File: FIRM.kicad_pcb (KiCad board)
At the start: 4 copper layers, 40.5 x 40.5 mm, 98 parts, among them J2 DM3CS-SF, Q2 IRLML6402, U1 STM32F405RGTx, U2 MIC5219-3.3YM5, U6 A-USBC-20F0-EA-GSR05, U7 W25Q128JVS, X2 32.768khz, Y1 12 MHz

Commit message: sub 600
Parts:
- removed 3.3V: 3.3V Test Point, TestPoint:TestPoint_THTPad_1.5x1.5mm_Drill0.7mm
- removed A0: PA0 Test Point, TestPoint:TestPoint_THTPad_1.5x1.5mm_Drill0.7mm
- removed A1: PA1 Test Point, TestPoint:TestPoint_THTPad_1.5x1.5mm_Drill0.7mm
- removed A10: PA10 Test Point, TestPoint:TestPoint_THTPad_1.5x1.5mm_Drill0.7mm
- removed A15: PA15 Test Point, TestPoint:TestPoint_THTPad_1.5x1.5mm_Drill0.7mm
- removed A2: PA2 Test Point, TestPoint:TestPoint_THTPad_1.5x1.5mm_Drill0.7mm
- removed A3: PA3 Test Point, TestPoint:TestPoint_THTPad_1.5x1.5mm_Drill0.7mm
- removed A4: PA4 Test Point, TestPoint:TestPoint_THTPad_1.5x1.5mm_Drill0.7mm
- removed A8: PA8 Test Point, TestPoint:TestPoint_THTPad_1.5x1.5mm_Drill0.7mm
- removed A9: PA9 Test Point, TestPoint:TestPoint_THTPad_1.5x1.5mm_Drill0.7mm
- removed B10: PB10 Test Point, TestPoint:TestPoint_THTPad_1.5x1.5mm_Drill0.7mm
- removed B11: PB11 Test Point, TestPoint:TestPoint_THTPad_1.5x1.5mm_Drill0.7mm
- removed B3: PB3 Test Point, TestPoint:TestPoint_THTPad_1.5x1.5mm_Drill0.7mm
- removed B4: PB4 Test Point, TestPoint:TestPoint_THTPad_1.5x1.5mm_Drill0.7mm
- removed B5: PB5 Test Point, TestPoint:TestPoint_THTPad_1.5x1.5mm_Drill0.7mm
- removed B8: PB8 Test Point, TestPoint:TestPoint_THTPad_1.5x1.5mm_Drill0.7mm
- removed BAT: Conn_01x02_Pin, Connector_PinHeader_2.54mm:PinHeader_1x02_P2.54mm_Vertical
- removed BOOT0: BOOT0 Pad, TestPoint:TestPoint_Pad_1.5x1.5mm
- removed C0: PC0 Test Point, TestPoint:TestPoint_THTPad_1.5x1.5mm_Drill0.7mm
- removed the C13 at (101.5, 107.0)
- removed the C13 at (117.9, 114.3)
- removed GND (x2): GND Test Point, TestPoint:TestPoint_THTPad_1.5x1.5mm_Drill0.7mm
- removed GND: GND Through-Hole, TestPoint:TestPoint_THTPad_1.5x1.5mm_Drill0.7mm
- removed MOSI: SPI_SDI, Jumper:SolderJumper-2_P1.3mm_Open_RoundedPad1.0x1.5mm
- removed Q2: IRLML6402, Package_TO_SOT_SMD:SOT-23
- removed R22: 5.1k, Resistor_SMD:R_0603_1608Metric
- removed RST: PTS815, Button_Switch_SMD:SW_SPST_PTS810
- removed SCK: SPI_SCK, Jumper:SolderJumper-2_P1.3mm_Open_RoundedPad1.0x1.5mm
- removed SCL: I2C_SCL, Jumper:SolderJumper-2_P1.3mm_Open_RoundedPad1.0x1.5mm
- removed SDA: I2C_SDA, Jumper:SolderJumper-2_P1.3mm_Open_RoundedPad1.0x1.5mm
- removed SWCLK: SWCLK Through-Hole, TestPoint:TestPoint_THTPad_1.5x1.5mm_Drill0.7mm
- removed SWDIO: SWDIO Through-Hole, TestPoint:TestPoint_THTPad_1.5x1.5mm_Drill0.7mm
- removed TP30: PC1 Test Point, TestPoint:TestPoint_THTPad_1.5x1.5mm_Drill0.7mm
- removed X2: 32.768khz, Crystal:Crystal_SMD_3215-2Pin_3.2x1.5mm
- added C13: 100n, Capacitor_SMD:C_0402_1005Metric, F.Cu at (126.0, 68.8)
- added C28: 10u, Capacitor_SMD:C_0402_1005Metric, F.Cu at (131.5, 83.4)
- added C29: 1u, Capacitor_SMD:C_0402_1005Metric, F.Cu at (131.5, 85.3)
- added C30: 10u, Capacitor_SMD:C_0402_1005Metric, F.Cu at (131.5, 87.3)
- added J1: DM3CS-SF, connectors:HRS_DM3CS-SF, B.Cu at (160.7, 88.9)
- added Q1: IRLML6402, Package_TO_SOT_SMD:SOT-23, F.Cu at (165.5, 94.0)
- added R16: 100k, Resistor_SMD:R_0402_1005Metric, F.Cu at (131.8, 91.3)
- added R17: 0.01R, Resistor_SMD:R_0402_1005Metric, F.Cu at (131.8, 93.3)
- added TP1: PA0 Test Point, connectors:Testpoint_1.5x1.5mm_1.0mm, F.Cu at (173.7, 75.7)
- added TP10: I2C1_SCL Test Point, connectors:smd_test_pads_1mm, F.Cu at (136.6, 89.4)
- added TP11: I2C1_SDA Test Point, connectors:smd_test_pads_1mm, F.Cu at (136.6, 91.6)
- added TP12: SWDIO Through-Hole, connectors:Testpoint_1.5x1.5mm_1.0mm, F.Cu at (173.7, 85.9)
- added TP13: SWCLK Through-Hole, connectors:Testpoint_1.5x1.5mm_1.0mm, F.Cu at (173.7, 83.3)
- added TP14: 3.3V Test Point, connectors:Testpoint_1.5x1.5mm_1.0mm, F.Cu at (173.7, 96.0)
- added TP15: GND Test Point, connectors:Testpoint_1.5x1.5mm_1.0mm, F.Cu at (173.7, 88.4)
- added TP16: IMU_CS Test Point, connectors:smd_test_pads_1mm, F.Cu at (136.6, 93.9)
- added TP17: BMP_CS Test Point, connectors:smd_test_pads_1mm, F.Cu at (136.6, 96.1)
- added TP18: MAG_CS Test Point, connectors:smd_test_pads_1mm, F.Cu at (138.8, 89.4)
- added TP19: HIG_CS Test Point, connectors:smd_test_pads_1mm, F.Cu at (138.8, 91.6)
- added TP2: PA1 Test Point, connectors:Testpoint_1.5x1.5mm_1.0mm, F.Cu at (173.7, 78.3)
- added TP20: IMU_INT Test Point, connectors:smd_test_pads_1mm, F.Cu at (138.8, 93.9)
- added TP21: BMP_INT Test Point, connectors:smd_test_pads_1mm, F.Cu at (138.8, 96.1)
- added TP22: MAG_INT Test Point, connectors:smd_test_pads_1mm, F.Cu at (141.1, 89.4)
- added TP23: HIG_INT Test Point, connectors:smd_test_pads_1mm, F.Cu at (141.1, 91.6)
- added TP24: NRST Pad, connectors:smd_test_pads_1mm, F.Cu at (141.1, 93.9)
- added TP25: BOOT0 Pad, connectors:smd_test_pads_1mm, F.Cu at (141.1, 96.1)
- added TP3: PA2 Test Point, connectors:Testpoint_1.5x1.5mm_1.0mm, F.Cu at (173.7, 80.8)
- added TP4: PA9 Test Point, connectors:Testpoint_1.5x1.5mm_1.0mm, F.Cu at (173.7, 93.5)
- added TP5: PA10 Test Point, connectors:Testpoint_1.5x1.5mm_1.0mm, F.Cu at (173.7, 91.0)
- added TP6: PA4 Test Point, connectors:smd_test_pads_1mm, F.Cu at (134.4, 89.4)
- added TP7: MOSI2 Test Point, connectors:smd_test_pads_1mm, F.Cu at (134.4, 91.6)
- added TP8: MISO2 Test Point, connectors:smd_test_pads_1mm, F.Cu at (134.4, 93.9)
- added TP9: SCK2 Test Point, connectors:smd_test_pads_1mm, F.Cu at (134.4, 96.1)
- added U8: ~, sensors:IC_MMC5983MA, F.Cu at (170.8, 78.5)
- added U9: A-USBC-20F0-EA-GSR05, connectors:A-USBC-20F0-EA-GSR05, F.Cu at (163.9, 100.5)
- added X1: 32.768khz, Crystal:Crystal_SMD_3215-2Pin_3.2x1.5mm, F.Cu at (159.1, 75.8)
- C1: value 100n -> 0.1u; footprint Capacitor_SMD:C_0603_1608Metric -> Capacitor_SMD:C_0402_1005Metric
- C10: value 2u2 -> 14p; footprint Capacitor_SMD:C_0603_1608Metric -> Capacitor_SMD:C_0402_1005Metric
- C11, C12: value 6p -> 100n; footprint Capacitor_SMD:C_0603_1608Metric -> Capacitor_SMD:C_0402_1005Metric
- C14: value 14p -> 2u2; footprint Capacitor_SMD:C_0603_1608Metric -> Capacitor_SMD:C_0402_1005Metric
- C15, C8: value 0.1u -> 100n; footprint Capacitor_SMD:C_0603_1608Metric -> Capacitor_SMD:C_0402_1005Metric
- C16: value 1u -> 10n; footprint Capacitor_SMD:C_0603_1608Metric -> Capacitor_SMD:C_0402_1005Metric
- C17: value 10u -> 0.1u; footprint Capacitor_SMD:C_0603_1608Metric -> Capacitor_SMD:C_0402_1005Metric
- C18, C19, C20, C21, C24, C25, C27, C3, C9: footprint Capacitor_SMD:C_0603_1608Metric -> Capacitor_SMD:C_0402_1005Metric
- C2: value 100n -> 4u7; footprint Capacitor_SMD:C_0603_1608Metric -> Capacitor_SMD:C_0402_1005Metric
- C22: value 10u -> 100n; footprint Capacitor_SMD:C_0603_1608Metric -> Capacitor_SMD:C_0402_1005Metric
- C23: value 470p -> 100n; footprint Capacitor_SMD:C_0603_1608Metric -> Capacitor_SMD:C_0402_1005Metric
- C26: value 100n -> 470p; footprint Capacitor_SMD:C_0603_1608Metric -> Capacitor_SMD:C_0402_1005Metric
- C4: value 100n -> 6p; footprint Capacitor_SMD:C_0603_1608Metric -> Capacitor_SMD:C_0402_1005Metric
- C5: value 100n -> 14p; footprint Capacitor_SMD:C_0603_1608Metric -> Capacitor_SMD:C_0402_1005Metric
- C6: value 4u7 -> 100n; footprint Capacitor_SMD:C_0603_1608Metric -> Capacitor_SMD:C_0402_1005Metric
- C7: value 10n -> 6p; footprint Capacitor_SMD:C_0603_1608Metric -> Capacitor_SMD:C_0402_1005Metric
- D1: value D_Schottky -> LED_Blue; footprint Diode_SMD:D_SOD-123 -> LED_SMD:LED_0402_1005Metric
- D2: value LED -> LED_Yellow; footprint LED_SMD:LED_0805_2012Metric -> LED_SMD:LED_0402_1005Metric
- D3: value LED -> LED_Red; footprint LED_SMD:LED_0805_2012Metric -> LED_SMD:LED_0402_1005Metric
- D4: value LED -> D_Schottky; footprint LED_SMD:LED_0805_2012Metric -> Diode_SMD:D_SOD-123
- D5: value LED -> LED_Green; footprint LED_SMD:LED_0805_2012Metric -> LED_SMD:LED_0402_1005Metric
- J2: value DM3CS-SF -> Conn_01x02_Pin; footprint DM3CS-SF:HRS_DM3CS-SF -> connectors:power_headers; moved to F.Cu
- R1: value 100k -> 10k; footprint Resistor_SMD:R_0603_1608Metric -> Resistor_SMD:R_0402_1005Metric
- R10: value 330 -> 47k; footprint Resistor_SMD:R_0603_1608Metric -> Resistor_SMD:R_0402_1005Metric
- R11: value 1k2 -> 3k3; footprint Resistor_SMD:R_0603_1608Metric -> Resistor_SMD:R_0402_1005Metric
- R12: value 1k5 -> 3k3; footprint Resistor_SMD:R_0603_1608Metric -> Resistor_SMD:R_0402_1005Metric
- R13: value 10k -> 330; footprint Resistor_SMD:R_0603_1608Metric -> Resistor_SMD:R_0402_1005Metric; moved to B.Cu
- R14: value 10k -> 1k2; footprint Resistor_SMD:R_0603_1608Metric -> Resistor_SMD:R_0402_1005Metric; moved to B.Cu
- R15: value 1k2 -> 1k5; footprint Resistor_SMD:R_0603_1608Metric -> Resistor_SMD:R_0402_1005Metric; moved to B.Cu
- R18: value 2k2 -> 1k2; footprint Resistor_SMD:R_0603_1608Metric -> Resistor_SMD:R_0402_1005Metric
- R19: value 2k2 -> 100; footprint Resistor_SMD:R_0603_1608Metric -> Resistor_SMD:R_0402_1005Metric
- R2, R4, R7: footprint Resistor_SMD:R_0603_1608Metric -> Resistor_SMD:R_0402_1005Metric
- R20: value 100 -> 5.1k; footprint Resistor_SMD:R_0603_1608Metric -> Resistor_SMD:R_0402_1005Metric
- R21: value 10k -> 5.1k; footprint Resistor_SMD:R_0603_1608Metric -> Resistor_SMD:R_0402_1005Metric
- R3: value 47k -> 100k; footprint Resistor_SMD:R_0603_1608Metric -> Resistor_SMD:R_0402_1005Metric
- R5, R6: value 47k -> 10k; footprint Resistor_SMD:R_0603_1608Metric -> Resistor_SMD:R_0402_1005Metric
- R8: value 100k -> 47k; footprint Resistor_SMD:R_0603_1608Metric -> Resistor_SMD:R_0402_1005Metric
- R9: value 5.1k -> 47k; footprint Resistor_SMD:R_0603_1608Metric -> Resistor_SMD:R_0402_1005Metric
- U1: value STM32F405RGTx -> W25Q128JVS; footprint Package_QFP:LQFP-64_10x10mm_P0.5mm -> Package_SO:SOIC-8_5.3x5.3mm_P1.27mm; moved to B.Cu
- U2: value MIC5219-3.3YM5 -> STM32F405RGTx; footprint Package_TO_SOT_SMD:SOT-23-5 -> Package_QFP:LQFP-64_10x10mm_P0.5mm
- U3: value ~ -> ADXL371; footprint sensors:IC_ICM-45686 -> Sensor_Motion:Analog_LGA-16_3.25x3mm_P0.5mm_LayoutBorder3x5y
- U4: footprint sensors:IC_MMC5983MA -> sensors:IC_ICM-45686
- U5: value ~ -> INA219AxDCN; footprint Package_LGA:ST_HLGA-10_2x2mm_P0.5mm_LayoutBorder3x2y -> Package_TO_SOT_SMD:SOT-23-8
- U6: value A-USBC-20F0-EA-GSR05 -> MIC5219-3.3YM5; footprint connectors:A-USBC-20F0-EA-GSR05 -> Package_TO_SOT_SMD:SOT-23-5
- U7: value W25Q128JVS -> ~; footprint Package_SO:SOIC-8_5.3x5.3mm_P1.27mm -> sensors:BMPFootprintNoSolderMask; moved to F.Cu
- moved U4 76.6 mm to (171.3, 89.5), turned to 135 degrees
- moved H1 76.3 mm to (165.8, 77.1)
- moved D2 70.7 mm to (162.1, 76.1), turned to 0 degrees
- moved D3 69.2 mm to (162.0, 75.2), turned to 0 degrees
- moved H3 69.1 mm to (172.0, 99.1)
- moved R15 65.5 mm to (165.6, 80.1), turned to 0 degrees
- moved U3 64.0 mm to (170.7, 84.7), turned to -135 degrees
- moved J2 63.7 mm to (172.0, 93.0), turned to 0 degrees
- moved D1 63.1 mm to (162.1, 77.0)
- moved D5 59.9 mm to (166.9, 92.1), turned to 90 degrees
- moved C19 58.2 mm to (128.6, 77.5), turned to 0 degrees
- moved D4 56.3 mm to (161.0, 94.8), turned to 0 degrees
- moved C22 55.0 mm to (128.6, 83.4), turned to 0 degrees
- moved U5 54.2 mm to (169.2, 93.7), turned to 90 degrees
- moved C26 53.5 mm to (131.5, 79.4), turned to 0 degrees
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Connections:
- C1 pad 1: +3.3V -> /NRST
- C10 pad 1: /VCAP2 -> /HSE_OUT
- C11 pad 1: /LSE_IN -> GND
- C11 pad 2: GND -> +3.3V
- C12 pad 1: /LSE_OUT -> GND
- C12 pad 2: GND -> +3.3V
- C14 pad 1: /HSE_OUT -> /VCAP2
- C15 pad 1: /NRST -> +3.3V
- C16 pad 1: +3.3V -> Net-(U2-VDDA)
- C17 pad 1: GND -> Net-(U2-VDDA)
- C17 pad 2: Net-(U4-CAP) -> GND
- C19 pad 1: +3.3V -> GND
- C19 pad 2: GND -> +3.3V
- C20 pad 1: +3.3V -> GND
- C20 pad 2: GND -> +3.3V
- C21 pad 1: GND -> +3.3V
- C21 pad 2: +3.3V -> GND
- C22 pad 1: Net-(D1-K) -> +3.3V
- C23 pad 1: Net-(U2-BP) -> GND
- C23 pad 2: GND -> +3.3V
- C24 pad 1: +3.3V -> /VSENS_OUT
- C26 pad 1: GND -> Net-(U6-BP)
- C26 pad 2: +3.3V -> GND
- C4 pad 1: +3.3V -> /LSE_IN
- C5 pad 1: +3.3V -> /HSE_IN
- C7 pad 1: Net-(U1-VDDA) -> /LSE_OUT
- C8 pad 1: Net-(U1-VDDA) -> +3.3V
- D1 pad 1: Net-(D1-K) -> GND
- D1 pad 2: VBUS -> Net-(D1-A)
- D4 pad 1: GND -> /VSENS_IN
- D4 pad 2: Net-(D4-A) -> VBUS
- FB1 pad 1: Net-(U1-VDDA) -> Net-(U2-VDDA)
- J2 pad 1: /SDIO_D2 -> VBAT
- J2 pad 2: /SDIO_D3 -> GND
- R1 pad 1: /BOOT0 -> +3.3V
- R1 pad 2: GND -> Net-(U1-~{HOLD}/~{RESET}/IO_{3})
- R10 pad 1: Net-(D2-A) -> /SDIO_D2
- R10 pad 2: /DBUG_0 -> +3.3V
- R11 pad 1: Net-(D3-A) -> /I2C1_SCL
- R11 pad 2: /DBUG_1 -> +3.3V
- R12 pad 1: Net-(D4-A) -> /I2C1_SDA
- R12 pad 2: /DBUG_2 -> +3.3V
- R13 pad 1: +3.3V -> Net-(D1-A)
- R13 pad 2: Net-(U7-~{HOLD}/~{RESET}/IO_{3}) -> /DBUG_0
- R14 pad 1: +3.3V -> Net-(D2-A)
- R14 pad 2: Net-(U7-~{WP}/IO_{2}) -> /DBUG_1
- R15 pad 1: Net-(D5-A) -> Net-(D3-A)
- R15 pad 2: +3.3V -> /DBUG_2
- R18 pad 1: /I2C1_SCL -> Net-(D5-A)
- R19 pad 1: /I2C1_SDA -> Net-(R19-Pad1)
- R19 pad 2: +3.3V -> /BOOT0
- R2 pad 1: /SDIO_D2 -> /SDIO_D1
- R20 pad 2: /BOOT0 -> GND
- R21 pad 1: +3.3V -> Net-(U9-CC2)
- R21 pad 2: /FLASH_CS -> GND
- R3 pad 1: /SDIO_D3 -> /BOOT0
- R3 pad 2: +3.3V -> GND
- R4 pad 1: /SDIO_CMD -> /SDIO_D0
- R5 pad 1: /SDIO_D0 -> +3.3V
- R5 pad 2: +3.3V -> Net-(U1-~{WP}/IO_{2})
- R6 pad 1: /SDIO_D1 -> +3.3V
- R6 pad 2: +3.3V -> /SD_DETECT
- R7 pad 2: /SD_DETECT -> /FLASH_CS
- R8 pad 1: VBUS -> /SDIO_CMD
- R8 pad 2: GND -> +3.3V
- R9 pad 1: Net-(U6-CC1) -> /SDIO_D3
- R9 pad 2: GND -> +3.3V
- U1 pad 1: +3.3V -> /FLASH_CS
- U1 pad 2: /PC13 -> /MISO1
- U1 pad 3: /LSE_IN -> Net-(U1-~{WP}/IO_{2})
- U1 pad 4: /LSE_OUT -> GND
- U1 pad 5: /HSE_IN -> /MOSI1
- U1 pad 6: /HSE_OUT -> /SCK1
- U1 pad 7: /NRST -> Net-(U1-~{HOLD}/~{RESET}/IO_{3})
- U1 pad 8: /PC0 -> +3.3V
- U2 pad 1: Net-(D1-K) -> +3.3V
- U2 pad 2: GND -> /PC13
- U2 pad 3: Net-(D1-K) -> /LSE_IN
- U2 pad 4: Net-(U2-BP) -> /LSE_OUT
- U2 pad 5: +3.3V -> /HSE_IN
- U3 pad 1: /MISO2 -> +3.3V
- U3 pad 11: unconnected-(U3-RESV/AUX1_SDO-Pad11) -> /HIG_INT
- U3 pad 12: /IMU_CS -> GND
- U3 pad 13: /SCK2 -> GND
- U3 pad 14: /MOSI2 -> +3.3V
- U3 pad 4: /IMU_INT -> /SCK2
- U3 pad 5: +3.3V -> unconnected-(U3-RES-Pad5)
- U3 pad 6: GND -> /MOSI2
- U3 pad 7: unconnected-(U3-RESV-Pad7) -> /MISO2
- U3 pad 8: +3.3V -> /HIG_CS
- U4 pad 1: Net-(JP3-A) -> /MISO2
- U4 pad 10: Net-(U4-CAP) -> unconnected-(U4-RESV/AUX1_CS-Pad10)
- U4 pad 11: GND -> unconnected-(U4-RESV/AUX1_SDO-Pad11)
- U4 pad 12: unconnected-(U4-NC-Pad12) -> /IMU_CS
- U4 pad 13: +3.3V -> /SCK2
- U4 pad 14: unconnected-(U4-NC-Pad14) -> /MOSI2
- U4 pad 2: +3.3V -> unconnected-(U4-RESV/AUX1_SDIO/AUX1_SDI/MAS_DA-Pad2)
- U4 pad 4: /MAG_CS -> /IMU_INT
- U4 pad 5: /MISO2 -> +3.3V
- U4 pad 6: unconnected-(U4-NC-Pad6) -> GND
- U4 pad 8: unconnected-(U4-NC-Pad8) -> +3.3V
- U4 pad 9: GND -> unconnected-(U4-INT2/FSYNC/CLKIN-Pad9)
- U5 pad 1: +3.3V -> /VSENS_IN
- U5 pad 2: /SCK2 -> /VSENS_OUT
- U5 pad 4: /MOSI2 -> +3.3V
- U5 pad 5: /MISO2 -> /I2C1_SCL
- U5 pad 6: /BMP_CS -> /I2C1_SDA
- U5 pad 7: /BMP_INT -> GND
- U7 pad 1: /FLASH_CS -> +3.3V
- U7 pad 2: /MISO1 -> /SCK2
- U7 pad 3: Net-(U7-~{WP}/IO_{2}) -> GND
- U7 pad 4: GND -> /MOSI2
- U7 pad 5: /MOSI1 -> /MISO2
- U7 pad 6: /SCK1 -> /BMP_CS
- U7 pad 7: Net-(U7-~{HOLD}/~{RESET}/IO_{3}) -> /BMP_INT
- U7 pad 8: +3.3V -> GND
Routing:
- net GND: track 94.7 -> 0.00 mm, vias 47 -> 0
- net /MOSI2: track 66.4 -> 0.00 mm, vias 3 -> 0
- net /PA8: track 65.2 -> 0.00 mm, vias 7 -> 0
- net /MISO2: track 62.5 -> 0.00 mm, vias 2 -> 0
- net +3.3V: track 56.0 -> 0.00 mm, vias 33 -> 0
- net /I2C1_SCL: track 55.9 -> 0.00 mm, vias 5 -> 0
- net /SCK2: track 50.0 -> 0.00 mm, vias 3 -> 0
- net /I2C1_SDA: track 47.7 -> 0.00 mm, vias 7 -> 0
- net /PA1: track 45.6 -> 0.00 mm, vias 5 -> 0
- net /MAG_CS: track 41.4 -> 0.00 mm, vias 2 -> 0
- net /PB10: track 41.1 -> 0.00 mm, vias 2 -> 0
- net /PB11: track 39.9 -> 0.00 mm, vias 2 -> 0
- net /SDIO_D1: track 39.6 -> 0.00 mm, vias 3 -> 0
- net /SDIO_D0: track 37.7 -> 0.00 mm, vias 3 -> 0
- net /DBUG_0: track 37.3 -> 0.00 mm, vias 4 -> 0
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- removed copper zone on In2.Cu, net +3.3V
- removed copper zone on In1.Cu, net GND
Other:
- board size 40.5 x 40.5 mm -> 21.1 x 26.9 mm

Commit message: okay
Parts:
- C1, C11, C14, C22, C25, C26, C27, C3, C6, C8, R1, R10, R11, R12, R16, R17, R2, R20, R21, R3, R4, R5, R8, R9, TP10, TP25, U5: moved to B.Cu
- moved C13 52.0 mm to (170.3, 96.0), turned to -90 degrees
- moved C6 51.1 mm to (171.1, 84.5)
- moved C2 47.8 mm to (166.3, 91.4)
- moved C9 46.5 mm to (169.1, 86.5), turned to -45 degrees
- moved C19 45.7 mm to (172.1, 91.6), turned to 180 degrees
- moved C8 45.2 mm to (164.2, 97.9), turned to -90 degrees
- moved C20 45.1 mm to (172.5, 90.1), turned to 90 degrees
- moved C3 44.7 mm to (164.7, 80.1)
- moved R4 44.3 mm to (169.2, 85.5)
- moved C21 44.0 mm to (172.5, 84.4), turned to 135 degrees
- moved C23 44.0 mm to (172.5, 88.3), turned to -90 degrees
- moved R2 43.8 mm to (169.2, 84.5)
- moved C1 43.7 mm to (163.6, 81.0)
- moved C24 42.2 mm to (170.5, 92.7), turned to -90 degrees
- moved R12 42.1 mm to (169.7, 86.9), turned to 90 degrees
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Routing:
- net /HSE_IN: track 0.00 -> 4.11 mm

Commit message: finished routing
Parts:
- removed C3, C6: 100n, Capacitor_SMD:C_0402_1005Metric
- C15, C24, C28, TP11, TP16, TP17, TP19, TP22, TP24, TP6, TP8: moved to B.Cu
- R17: moved to F.Cu
- moved TP25 25.2 mm to (163.1, 100.5)
- moved TP16 23.0 mm to (167.5, 99.4), turned to 180 degrees
- moved TP19 17.8 mm to (169.0, 97.8), turned to 180 degrees
- moved TP11 15.6 mm to (169.1, 75.3), turned to 180 degrees
- moved TP20 13.7 mm to (160.5, 93.0)
- moved C9 12.6 mm to (157.9, 92.4), turned to 135 degrees
- moved TP10 11.5 mm to (167.9, 75.3)
- moved TP24 8.59 mm to (164.8, 100.5), turned to 180 degrees
- moved TP6 8.28 mm to (160.3, 99.4), turned to 180 degrees
- moved TP8 6.95 mm to (168.9, 80.5), turned to 180 degrees
- moved C14 6.64 mm to (168.7, 86.9), turned to 90 degrees
- moved TP18 5.54 mm to (172.4, 75.3)
- moved C15 5.09 mm to (166.9, 80.2), turned to 45 degrees
- moved C28 4.45 mm to (158.7, 97.1), turned to 180 degrees
- moved R11 3.99 mm to (172.5, 85.5)
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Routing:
- net GND: track 0.00 -> 151.0 mm, vias 0 -> 12
- net +3.3V: track 0.00 -> 92.8 mm, vias 0 -> 17
- net /SCK2: track 0.00 -> 49.8 mm, vias 0 -> 3
- net /MISO2: track 0.00 -> 40.4 mm, vias 0 -> 5
- net /IMU_CS: track 0.00 -> 39.1 mm, vias 0 -> 3
- net /MOSI2: track 0.00 -> 37.8 mm, vias 0 -> 4
- net /I2C1_SCL: track 0.00 -> 35.1 mm, vias 0 -> 3
- net /BMP_INT: track 0.00 -> 31.5 mm, vias 0 -> 3
- net /I2C1_SDA: track 0.00 -> 31.0 mm, vias 0 -> 3
- net /NRST: track 0.00 -> 29.5 mm, vias 0 -> 2
- net /FLASH_CS: track 0.00 -> 27.1 mm, vias 0 -> 3
- net /MAG_CS: track 0.00 -> 25.8 mm, vias 0 -> 2
- net /IMU_INT: track 0.00 -> 25.7 mm, vias 0 -> 2
- net Net-(R19-Pad1): track 0.00 -> 24.2 mm, vias 0 -> 2
- net /SDIO_D2: track 0.00 -> 23.5 mm, vias 0 -> 2
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- added copper zone on In2.Cu, net +3.3V
- added copper zone on In1.Cu, net GND
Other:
- copper layers 4 -> 8

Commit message: byebye drc errors
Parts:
- moved TP11 0.93 mm to (169.5, 76.1)
- moved TP10 0.61 mm to (168.4, 75.6)
- moved C24 0.36 mm to (172.3, 90.7)
- moved TP17 0.24 mm to (169.1, 82.1)
- moved TP18 0.22 mm to (172.4, 75.5)
- moved R19 0.05 mm to (153.9, 82.1)
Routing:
- net Net-(U1-~{HOLD}/~{RESET}/IO_{3}): track 4.36 -> 10.6 mm, vias 2 -> 0
- net GND: track 151.0 -> 155.1 mm
- net +3.3V: track 92.8 -> 94.3 mm
- net /I2C1_SDA: track 31.0 -> 30.3 mm
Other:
- board size 21.1 x 26.9 mm -> 21.3 x 27 mm

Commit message: cleanup
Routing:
- net GND: track 155.1 -> 156.6 mm, vias 12 -> 13
- net /MISO2: track 40.4 -> 39.8 mm
- net /IMU_CS: track 39.1 -> 38.6 mm
- net /MAG_CS: track 25.4 -> 24.9 mm

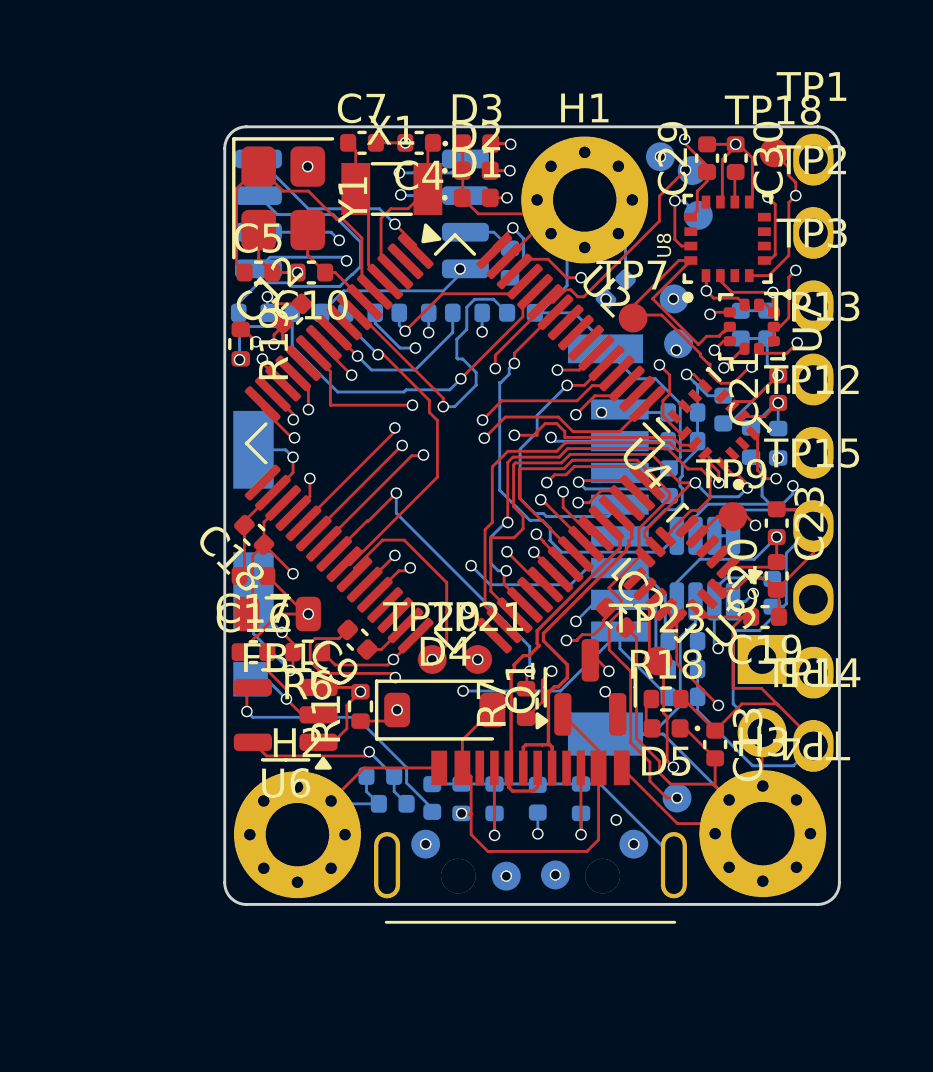
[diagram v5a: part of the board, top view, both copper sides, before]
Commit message: add back decoupling capacitors for stm
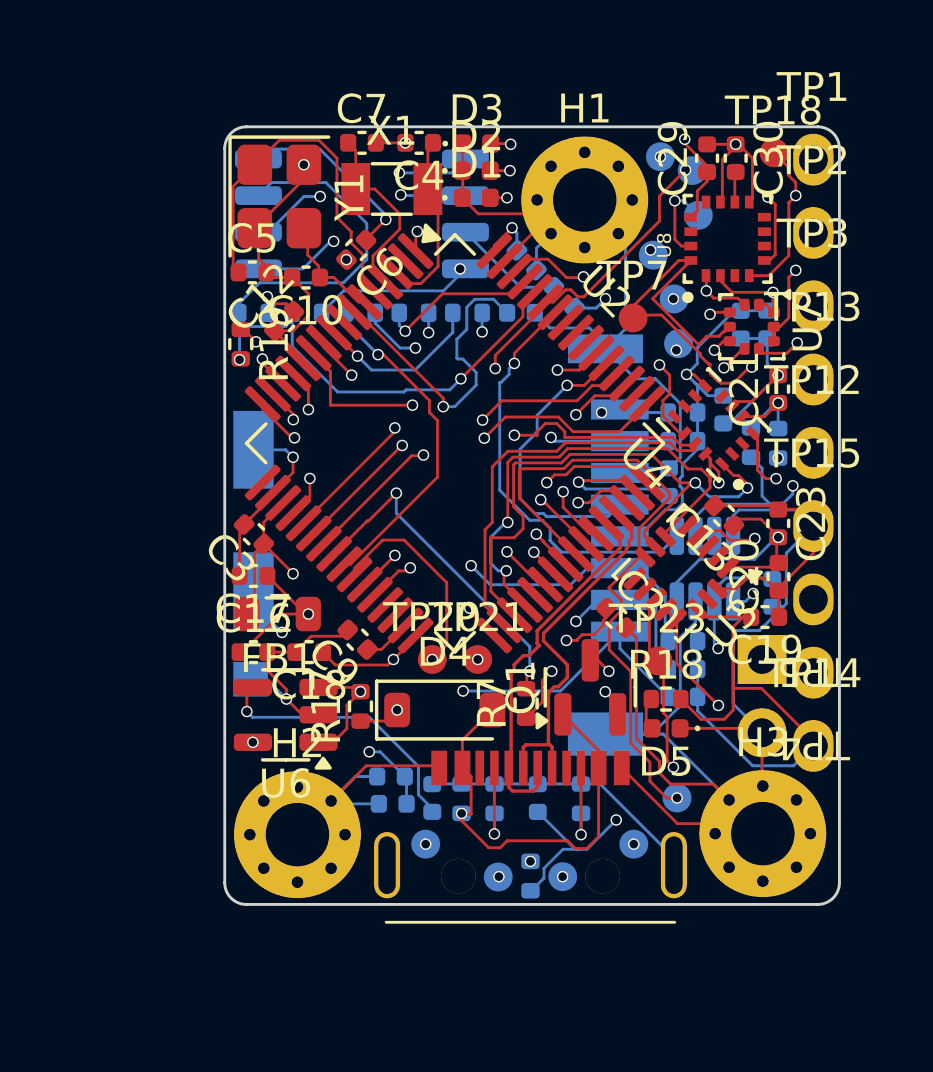
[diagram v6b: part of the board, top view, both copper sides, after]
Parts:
- added C3: 100n, Capacitor_SMD:C_0402_1005Metric, F.Cu at (154.3, 88.7)
- added C6: 100n, Capacitor_SMD:C_0402_1005Metric, F.Cu at (157.9, 78.8)
- R6, TP9: moved to B.Cu
- moved R6 10.9 mm to (163.9, 100.5), turned to 90 degrees
- moved TP9 9.47 mm to (168.2, 79.0), turned to 180 degrees
- moved C13 7.94 mm to (170.6, 88.1), turned to 135 degrees
- moved C28 5.51 mm to (164.2, 97.8), turned to 90 degrees
- moved C8 5.15 mm to (159.1, 97.1), turned to 180 degrees
- moved C18 4.49 mm to (156.3, 92.8), turned to 180 degrees
- moved C15 3.25 mm to (163.8, 79.2), turned to -45 degrees
- moved R5 2.23 mm to (165.1, 80.5), turned to 135 degrees
- moved C12 0.38 mm to (155.4, 81.3)
- moved TP25 0.28 mm to (162.8, 100.6)
- moved TP24 0.26 mm to (165.1, 100.6)
- moved C10 0.25 mm to (156.2, 79.8)
- moved C5 0.21 mm to (154.3, 79.6)
- moved Y1 0.15 mm to (155.2, 77.0)
- moved C20 0.07 mm to (172.5, 90.2)
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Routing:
- net /SD_DETECT: track 14.8 -> 21.9 mm
- net GND: track 156.6 -> 152.2 mm, vias 13 -> 11
- net /SCK2: track 49.5 -> 52.2 mm, vias 3 -> 4
- net Net-(U1-~{WP}/IO_{2}): track 1.77 -> 3.85 mm
- net +3.3V: track 94.3 -> 96.1 mm, vias 17 -> 18
- net /USB_D-: track 13.6 -> 12.1 mm
- net /SDIO_D3: track 20.3 -> 18.9 mm
- net /VSENS_OUT: track 22.4 -> 21.3 mm
- net /HSE_IN: track 10.8 -> 11.9 mm
- net /MISO1: track 19.3 -> 20.4 mm
- net /SWDIO: track 11.2 -> 10.1 mm
- net /HIG_INT: track 23.0 -> 22.0 mm
- net /VSENS_IN: track 17.2 -> 16.3 mm
- net /SDIO_D1: track 10.1 -> 9.22 mm
- net /BOOT0: track 15.2 -> 14.4 mm
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
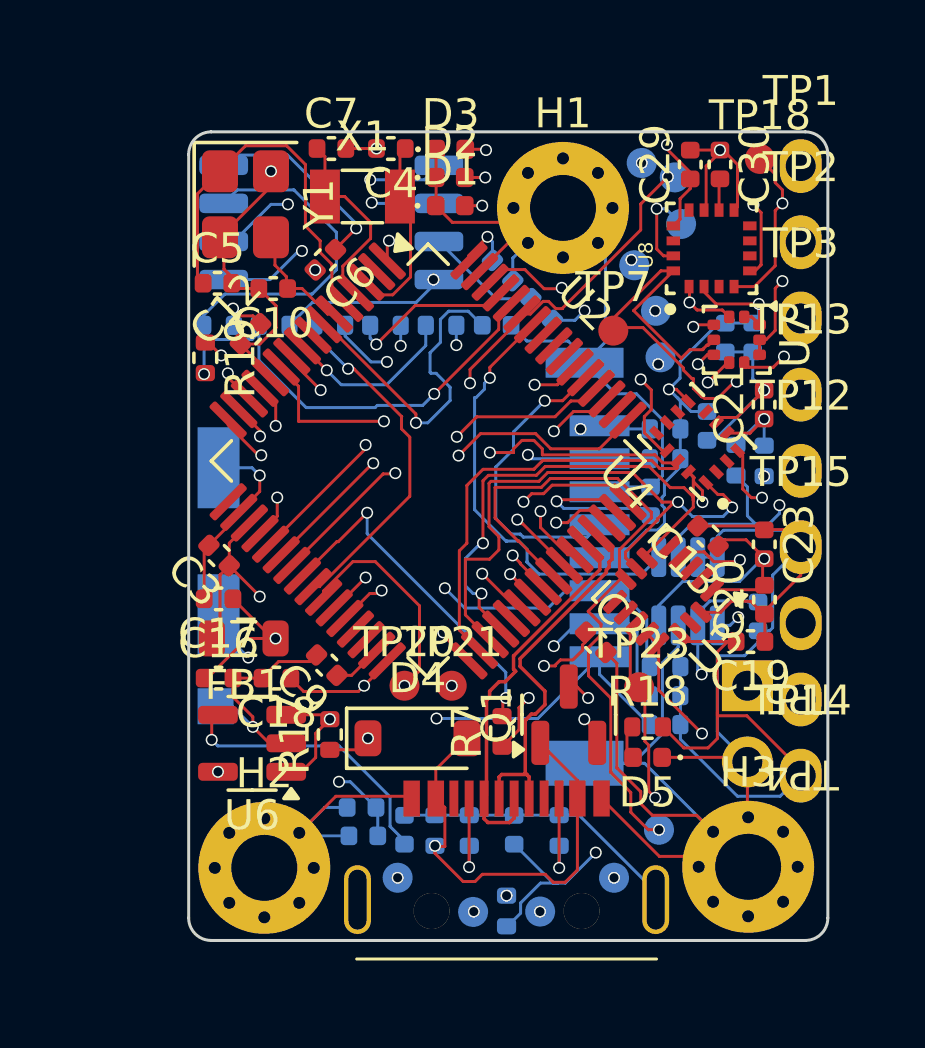
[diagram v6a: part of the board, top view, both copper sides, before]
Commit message: clean up and moved shunt resistor
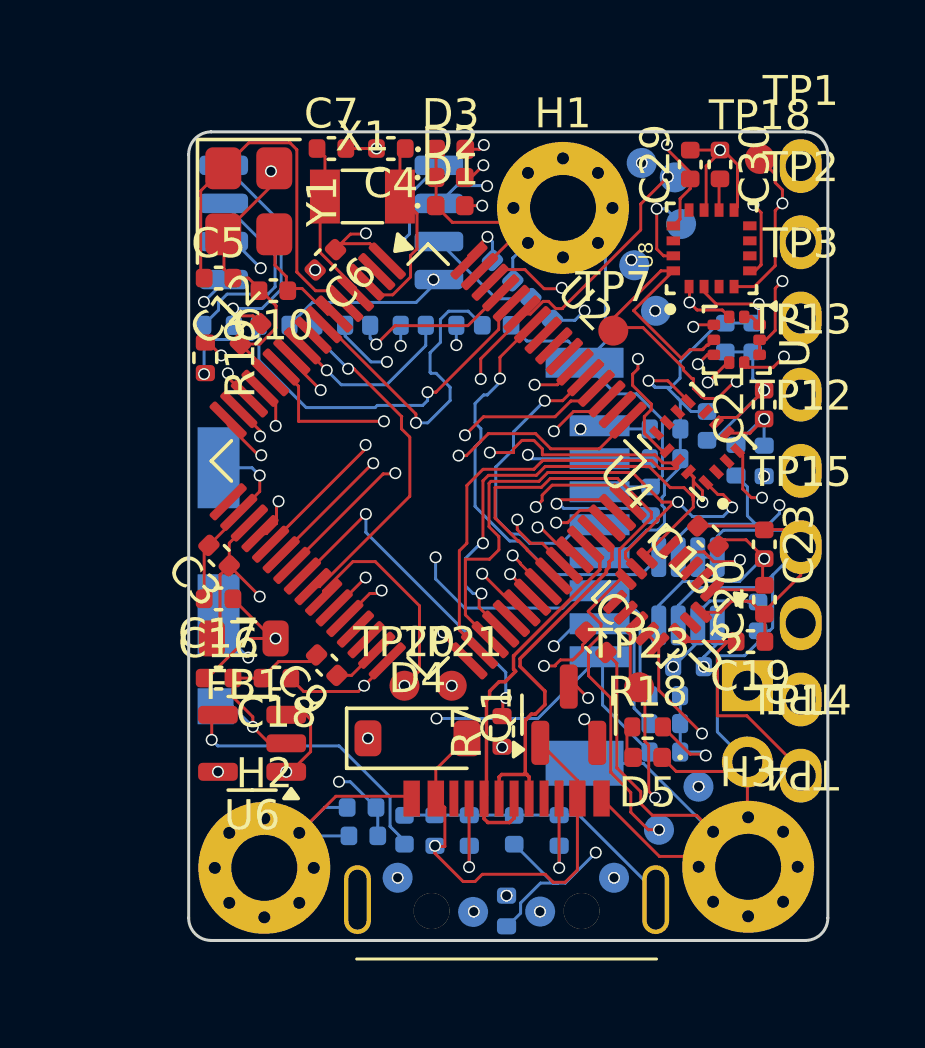
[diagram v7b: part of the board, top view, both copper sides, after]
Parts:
- R17: moved to B.Cu
- moved TP17 14.4 mm to (170.3, 96.4)
- moved R17 12.2 mm to (170.0, 92.4), turned to 180 degrees
- moved R8 0.96 mm to (169.2, 93.4)
- moved R9 0.93 mm to (169.2, 94.3)
- moved R10 0.91 mm to (169.2, 95.2)
- moved C5 0.18 mm to (154.3, 79.5)
- moved Y1 0.15 mm to (155.3, 76.9)
- moved C10 0.07 mm to (156.2, 79.9)
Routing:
- net /BMP_CS: track 16.0 -> 39.9 mm
- net Net-(U1-~{HOLD}/~{RESET}/IO_{3}): track 11.2 -> 6.56 mm
- net /SCK1: track 16.7 -> 13.4 mm
- net /MISO1: track 20.4 -> 17.1 mm
- net +3.3V: track 96.1 -> 93.0 mm
- net /MOSI1: track 17.0 -> 14.8 mm
- net GND: track 152.2 -> 150.0 mm
- net /FLASH_CS: track 27.1 -> 25.1 mm
- net /VSENS_IN: track 16.3 -> 14.3 mm
- net /SDIO_CMD: track 19.8 -> 21.6 mm
- net /SDIO_D2: track 22.8 -> 23.7 mm
- net /PA10: track 12.6 -> 11.7 mm
- net /SDIO_D3: track 18.9 -> 19.6 mm
- net /LSE_OUT: track 5.90 -> 5.25 mm
- net /I2C1_SCL: track 34.7 -> 34.1 mm

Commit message: stuff for willy boy
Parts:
- TP17, TP19: moved to F.Cu
- TP18, TP20, TP7: moved to B.Cu
- moved TP19 9.74 mm to (160.5, 93.0), turned to 0 degrees
- moved TP20 9.67 mm to (168.9, 97.8), turned to 180 degrees
- moved C2 9.28 mm to (158.1, 94.4), turned to -90 degrees
- moved TP7 1.10 mm to (167.8, 80.1), turned to 180 degrees
- moved R17 0.07 mm to (169.9, 92.4)
- turned TP17 to 0 degrees
- turned TP18 to 180 degrees
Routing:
- net /IMU_INT: track 25.7 -> 39.1 mm, vias 2 -> 3
- net GND: track 150.0 -> 142.1 mm, vias 11 -> 12
- net /HIG_CS: track 22.5 -> 20.6 mm, vias 1 -> 2
- net +3.3V: track 93.0 -> 91.5 mm
- net /MOSI2: track 36.6 -> 35.2 mm
- net /SCK2: track 52.2 -> 51.4 mm
- net /SD_DETECT: track 21.9 -> 22.5 mm
- net /HIG_INT: track 22.3 -> 21.7 mm
- net /BMP_INT: track 31.3 -> 30.7 mm
- net /I2C1_SDA: track 29.7 -> 29.1 mm
